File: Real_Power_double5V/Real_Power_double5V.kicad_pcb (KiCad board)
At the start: 4 copper layers, 92.3 x 114.5 mm, 90 parts, among them K1 RT314F05(gen), K2 RT314F05(gen), K3 RT314F05(gen), K4 RT314F05(gen), Q1 AOD4185, Q10 MMBT2222A, Q11 MMBT2222A, Q12 MMBT2222A, Q2 MMBT2222A, Q6 MMBT2222A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

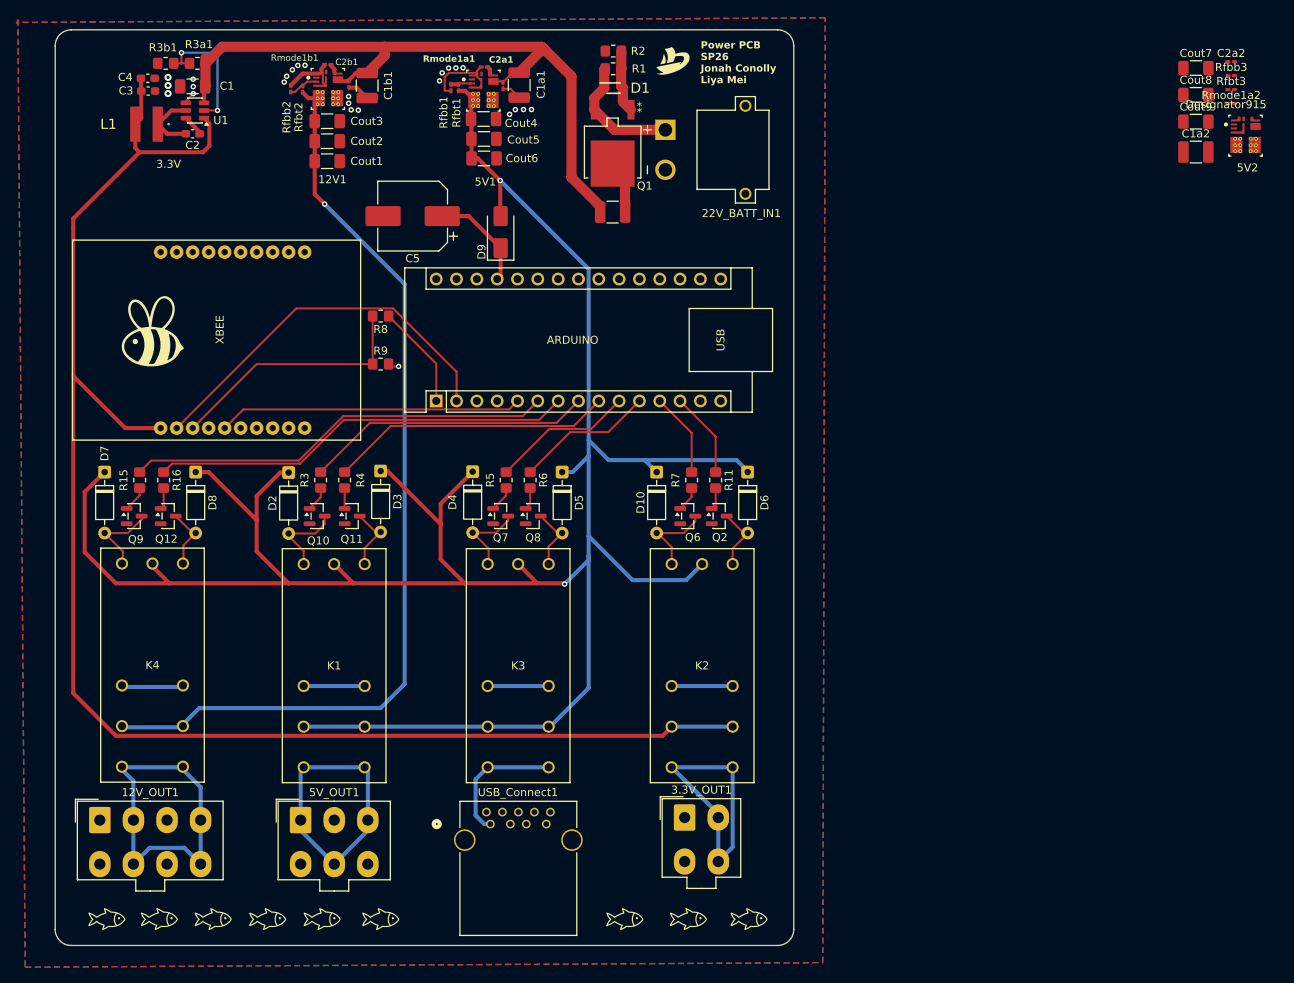
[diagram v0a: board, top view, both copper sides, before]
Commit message: added new 5V buck schematic
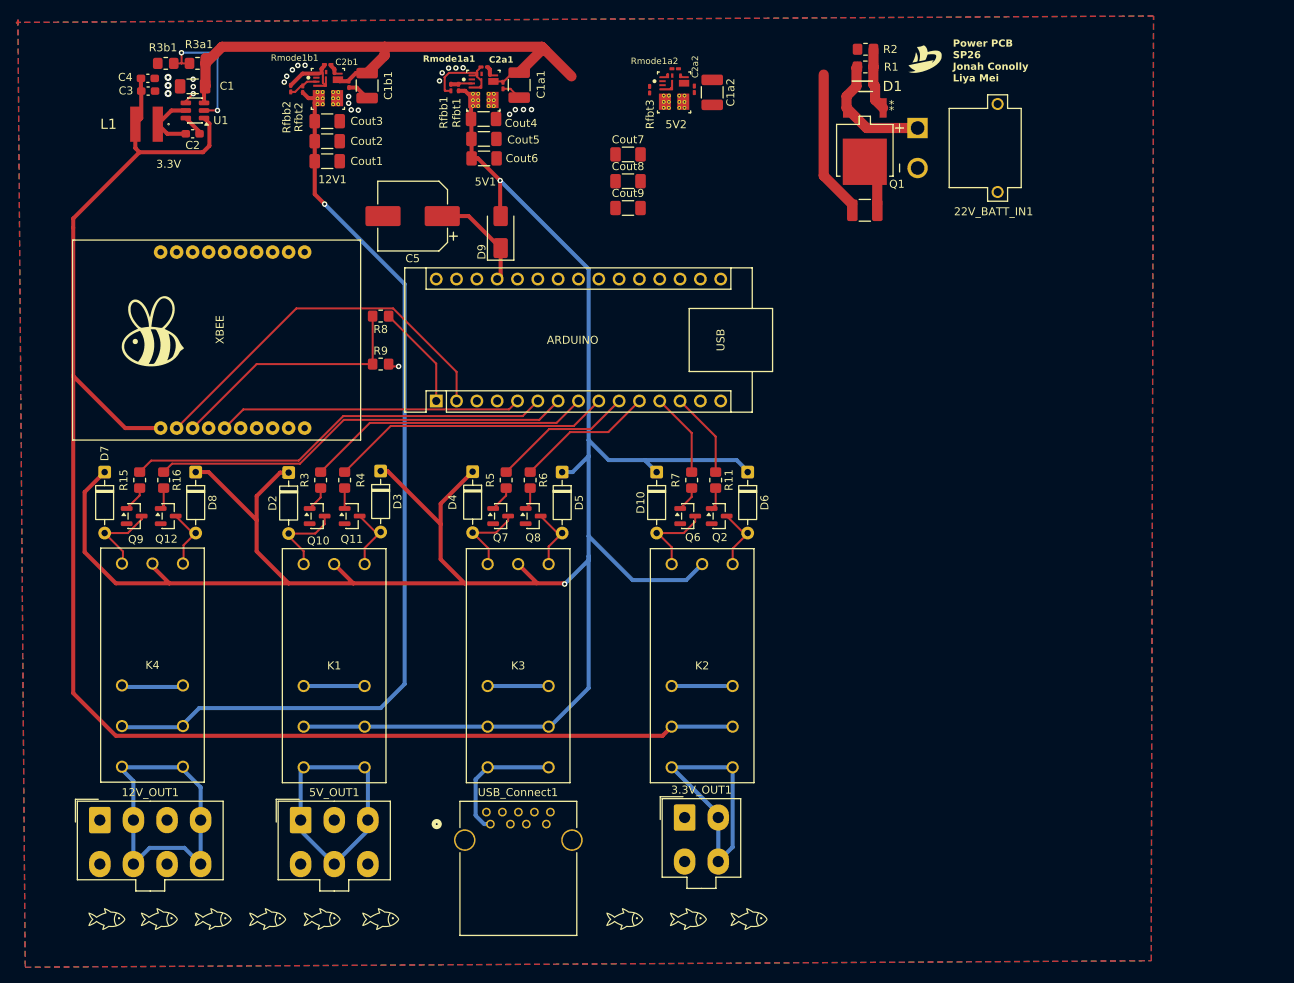
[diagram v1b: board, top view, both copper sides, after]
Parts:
- removed Rfbb3: 10k, Resistor_SMD:R_0201_0603Metric_Pad0.64x0.40mm_HandSolder
- moved Rfbt3 72.7 mm to (127.8, 51.9), turned to 90 degrees
- moved Cout7 71.8 mm to (125.1, 60.0)
- moved Cout8 71.8 mm to (125.1, 63.3)
- moved Cout9 71.8 mm to (125.1, 66.7)
- moved 5V2 71.6 mm to (130.9, 52.3)
- moved Rmode1a2 69.6 mm to (131.0, 49.3), turned to 180 degrees
- moved C2a2 67.2 mm to (133.4, 51.8), turned to -90 degrees
- moved C1a2 60.9 mm to (135.6, 52.2), turned to -90 degrees
- moved R2 31.5 mm to (154.8, 46.8)
- moved 22V_BATT_IN1 31.5 mm to (171.3, 59.2)
- moved G*** 31.5 mm to (162.3, 48.1)
- moved Main_Bulk(electrolytic)1 31.5 mm to (154.7, 67.0)
- moved Q1 31.5 mm to (154.7, 59.5)
- moved R1 31.5 mm to (154.8, 49.0)
- moved D1 31.5 mm to (154.8, 51.5)
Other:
- board outline removed
